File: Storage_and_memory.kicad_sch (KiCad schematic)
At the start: 19 parts, among them J4 DM3AT-SF-PEJM5, U14 SN74AVCA406DGGR, U15 W25Q256JVFIQ

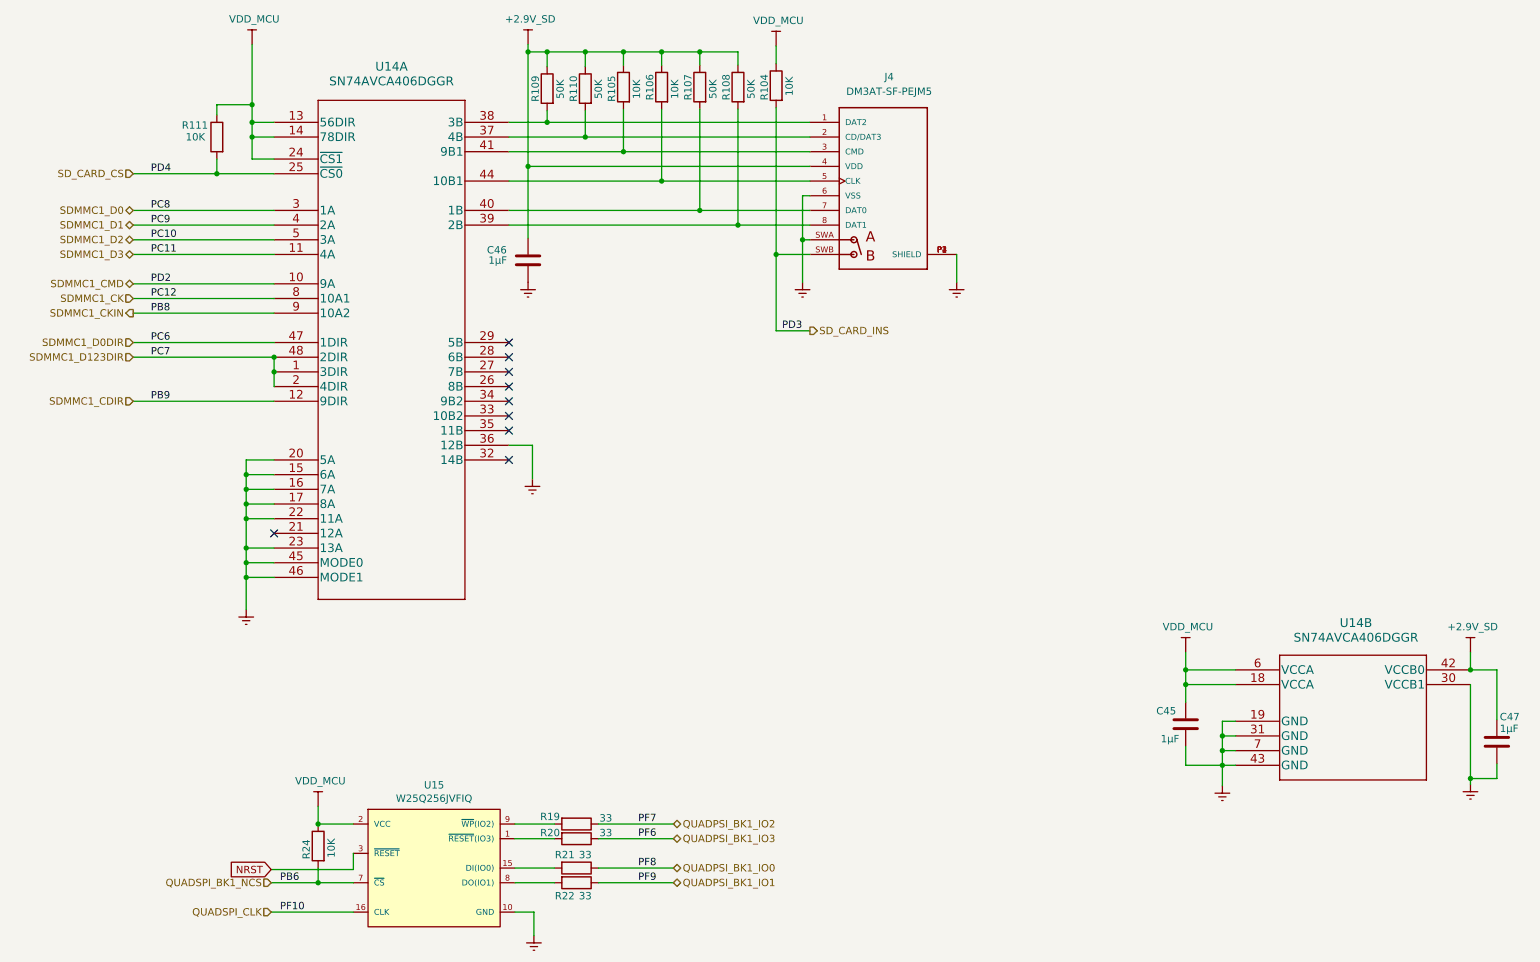
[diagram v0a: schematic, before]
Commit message: KiCAD6.0 scheema rules check done
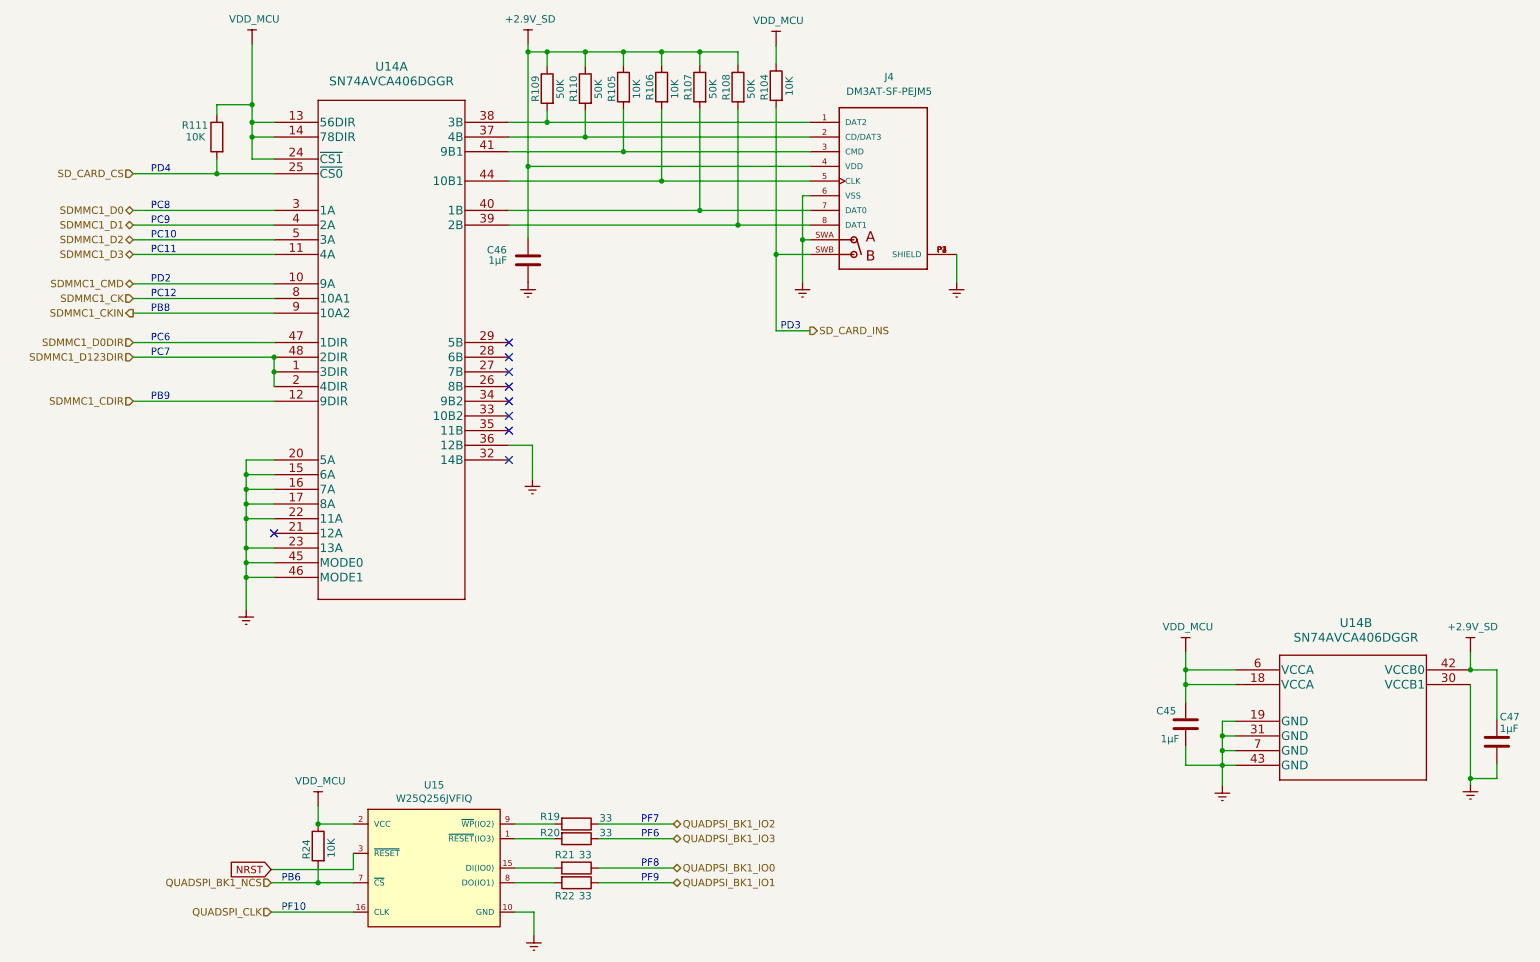
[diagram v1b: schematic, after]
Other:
- note added: "PB6"
- note added: "PB8"
- note added: "PB9"
- note added: "PC10"
- note added: "PC11"
- note added: "PC12"
- note added: "PC6"
- note added: "PC7"
- note added: "PC8"
- note added: "PC9"
- note added: "PD2"
- note added: "PD3"
- note added: "PD4"
- note added: "PF10"
- note added: "PF6"
- note added: "PF7"
- note added: "PF8"
- note added: "PF9"
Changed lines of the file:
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@@
     (stroke (width 0) (type default) (color 0 0 0 0))
   )
-  (label "PC9" (at 45.72 64.262 0)
+  (text "PF10" (at 68.326 183.134 0)
     (effects (font (size 1.27 1.27)) (justify left bottom))
   )
-  (label "PF7" (at 130.048 167.894 0)
+  (text "PD3" (at 154.686 82.55 0)
     (effects (font (size 1.27 1.27)) (justify left bottom))
   )
-  (label "PF9" (at 130.048 178.054 0)
+  (text "PC8" (at 45.72 61.722 0)
     (effects (font (size 1.27 1.27)) (justify left bottom))
   )
-  (label "PD2" (at 45.72 74.422 0)
+  (text "PB6" (at 68.326 178.054 0)
     (effects (font (size 1.27 1.27)) (justify left bottom))
   )
-  (label "PC6" (at 45.72 84.582 0)
+  (text "PC9" (at 45.72 64.262 0)
     (effects (font (size 1.27 1.27)) (justify left bottom))
   )
-  (label "PC11" (at 45.72 69.342 0)
+  (text "PF7" (at 130.556 167.894 0)
     (effects (font (size 1.27 1.27)) (justify left bottom))
   )
-  (label "PC7" (at 45.72 87.122 0)
+  (text "PF8" (at 130.556 175.514 0)
     (effects (font (size 1.27 1.27)) (justify left bottom))
   )
-  (label "PB9" (at 45.72 94.742 0)
+  (text "PF9" (at 130.556 178.054 0)
     (effects (font (size 1.27 1.27)) (justify left bottom))
   )
-  (label "PC8" (at 45.72 61.722 0)
+  (text "PD4" (at 45.72 55.372 0)
     (effects (font (size 1.27 1.27)) (justify left bottom))
   )
-  (label "PC10" (at 45.72 66.802 0)
+  (text "PC12" (at 45.72 76.962 0)
     (effects (font (size 1.27 1.27)) (justify left bottom))
   )
-  (label "PD3" (at 154.94 82.55 0)
+  (text "PF6" (at 130.556 170.434 0)
     (effects (font (size 1.27 1.27)) (justify left bottom))
   )
-  (label "PF8" (at 130.048 175.514 0)
+  (text "PD2" (at 45.72 74.422 0)
     (effects (font (size 1.27 1.27)) (justify left bottom))
   )
-  (label "PC12" (at 45.72 76.962 0)
+  (text "PB9" (at 45.72 94.742 0)
     (effects (font (size 1.27 1.27)) (justify left bottom))
   )
-  (label "PB6" (at 68.072 178.054 0)
+  (text "PC11" (at 45.72 69.342 0)
     (effects (font (size 1.27 1.27)) (justify left bottom))
   )
-  (label "PF10" (at 68.072 183.134 0)
+  (text "PB8" (at 45.72 79.502 0)
     (effects (font (size 1.27 1.27)) (justify left bottom))
   )
-  (label "PD4" (at 45.72 55.372 0)
+  (text "PC7" (at 45.72 87.122 0)
     (effects (font (size 1.27 1.27)) (justify left bottom))
   )
-  (label "PF6" (at 130.048 170.434 0)
+  (text "PC6" (at 45.72 84.582 0)
     (effects (font (size 1.27 1.27)) (justify left bottom))
   )
-  (label "PB8" (at 45.72 79.502 0)
+  (text "PC10" (at 45.72 66.802 0)
     (effects (font (size 1.27 1.27)) (justify left bottom))
   )

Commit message: PCB ver. 0.3
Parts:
- R104, R105, R106, R107, R108, R109, R110, R111: footprint Resistor_SMD:R_0805_2012Metric_Pad1.20x1.40mm_HandSolder -> Resistor_SMD:R_0805_2012Metric
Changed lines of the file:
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@@
       (effects (font (size 1.27 1.27)) (justify left))
     )
-    (property "Footprint" "Resistor_SMD:R_0805_2012Metric_Pad1.20x1.40mm_HandSolder" (id 2) (at 58.928 49.022 90)
+    (property "Footprint" "Resistor_SMD:R_0805_2012Metric" (id 2) (at 58.928 49.022 90)
       (effects (font (size 1.27 1.27)) hide)
     )
@@
       (effects (font (size 1.27 1.27)) (justify left))
     )
-    (property "Footprint" "Resistor_SMD:R_0805_2012Metric_Pad1.20x1.40mm_HandSolder" (id 2) (at 116.078 40.64 90)
+    (property "Footprint" "Resistor_SMD:R_0805_2012Metric" (id 2) (at 116.078 40.64 90)
       (effects (font (size 1.27 1.27)) hide)
     )
@@
       (effects (font (size 1.27 1.27)) (justify left))
     )
-    (property "Footprint" "Resistor_SMD:R_0805_2012Metric_Pad1.20x1.40mm_HandSolder" (id 2) (at 122.682 40.64 90)
+    (property "Footprint" "Resistor_SMD:R_0805_2012Metric" (id 2) (at 122.682 40.64 90)
       (effects (font (size 1.27 1.27)) hide)
     )
@@
       (effects (font (size 1.27 1.27)) (justify left))
     )
-    (property "Footprint" "Resistor_SMD:R_0805_2012Metric_Pad1.20x1.40mm_HandSolder" (id 2) (at 129.286 40.386 90)
+    (property "Footprint" "Resistor_SMD:R_0805_2012Metric" (id 2) (at 129.286 40.386 90)
       (effects (font (size 1.27 1.27)) hide)
     )
@@
       (effects (font (size 1.27 1.27)) (justify left))
     )
-    (property "Footprint" "Resistor_SMD:R_0805_2012Metric_Pad1.20x1.40mm_HandSolder" (id 2) (at 135.89 40.386 90)
+    (property "Footprint" "Resistor_SMD:R_0805_2012Metric" (id 2) (at 135.89 40.386 90)
       (effects (font (size 1.27 1.27)) hide)
     )
@@
       (effects (font (size 1.27 1.27)) (justify left))
     )
-    (property "Footprint" "Resistor_SMD:R_0805_2012Metric_Pad1.20x1.40mm_HandSolder" (id 2) (at 142.494 40.386 90)
+    (property "Footprint" "Resistor_SMD:R_0805_2012Metric" (id 2) (at 142.494 40.386 90)
       (effects (font (size 1.27 1.27)) hide)
     )
@@
       (effects (font (size 1.27 1.27)) (justify left))
     )
-    (property "Footprint" "Resistor_SMD:R_0805_2012Metric_Pad1.20x1.40mm_HandSolder" (id 2) (at 149.098 40.386 90)
+    (property "Footprint" "Resistor_SMD:R_0805_2012Metric" (id 2) (at 149.098 40.386 90)
       (effects (font (size 1.27 1.27)) hide)
     )
@@
       (effects (font (size 1.27 1.27)) (justify left))
     )
-    (property "Footprint" "Resistor_SMD:R_0805_2012Metric_Pad1.20x1.40mm_HandSolder" (id 2) (at 155.702 40.132 90)
+    (property "Footprint" "Resistor_SMD:R_0805_2012Metric" (id 2) (at 155.702 40.132 90)
       (effects (font (size 1.27 1.27)) hide)
     )

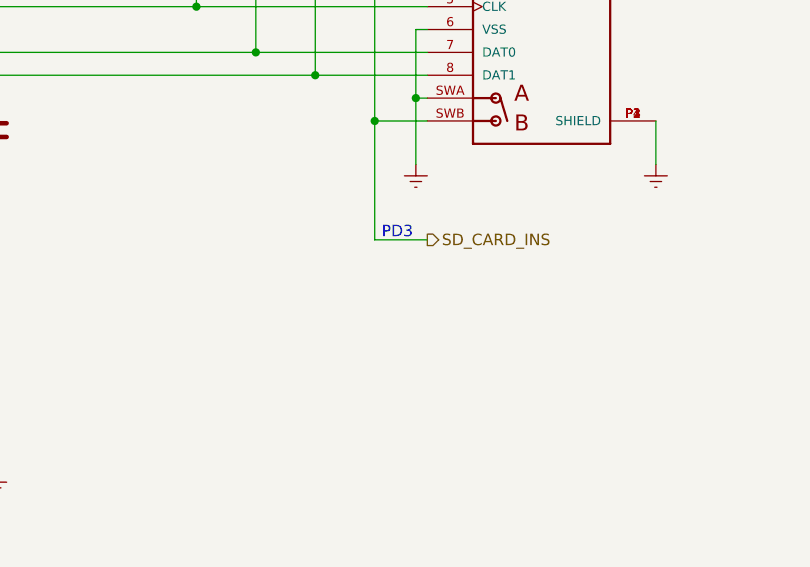
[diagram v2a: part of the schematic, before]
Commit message: GPIO port changed for input signals
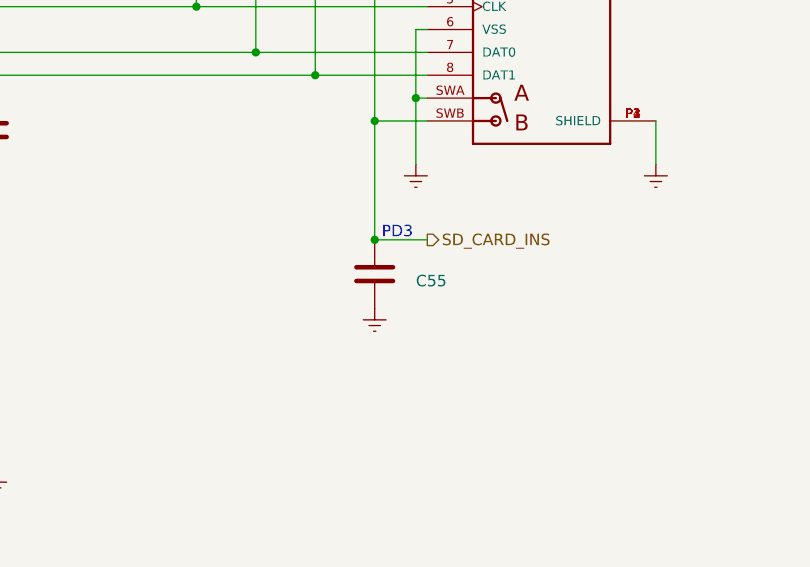
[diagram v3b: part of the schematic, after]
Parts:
- added C55: (no value), symbol Device:C
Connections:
- net GNDREF: now also C55.2
- net SD_CARD_INS: now also C55.1
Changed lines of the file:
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@@
   (junction (at 63.246 43.434) (diameter 0) (color 0 0 0 0)
+  )
+  (junction (at 153.924 82.55) (diameter 0) (color 0 0 0 0)
   )
   (junction (at 57.15 55.372) (diameter 0) (color 0 0 0 0)
@@
     (pin "8")
     (pin "9")
+    (pin "18")
+    (pin "19")
+    (pin "30")
+    (pin "31")
+    (pin "42")
+    (pin "43")
+    (pin "6")
+    (pin "7")
   )
   (symbol (lib_id "SVIELCOM_Library:SN74AVCA406DGGR") (at 233.426 143.764 0) (unit 2)
@@
       (effects (font (size 1.524 1.524)) hide)
     )
+    (pin "1")
+    (pin "10")
+    (pin "11")
+    (pin "12")
+    (pin "13")
+    (pin "14")
+    (pin "15")
+    (pin "16")
+    (pin "17")
+    (pin "2")
+    (pin "20")
+    (pin "21")
+    (pin "22")
+    (pin "23")
+    (pin "24")
+    (pin "25")
+    (pin "26")
+    (pin "27")
+    (pin "28")
+    (pin "29")
+    (pin "3")
+    (pin "32")
+    (pin "33")
+    (pin "34")
+    (pin "35")
+    (pin "36")
+    (pin "37")
+    (pin "38")
+    (pin "39")
+    (pin "4")
+    (pin "40")
+    (pin "41")
+    (pin "44")
+    (pin "45")
+    (pin "46")
+    (pin "47")
+    (pin "48")
+    (pin "5")
+    (pin "8")
+    (pin "9")
     (pin "18")
     (pin "19")
@@
     (pin "1")
   )
+  (symbol (lib_id "power:GNDREF") (at 153.924 90.17 0) (unit 1)
+    (in_bom yes) (on_board yes)
+    (property "Reference" "#PWR075" (id 0) (at 153.924 96.52 0)
+      (effects (font (size 1.27 1.27)) hide)
+    )
+    (property "Value" "GNDREF" (id 1) (at 154.051 93.4212 90)
+      (effects (font (size 1.27 1.27)) (justify right) hide)
+    )
+    (property "Footprint" "" (id 2) (at 153.924 90.17 0)
+      (effects (font (size 1.27 1.27)) hide)
+    )
+    (property "Datasheet" "" (id 3) (at 153.924 90.17 0)
+      (effects (font (size 1.27 1.27)) hide)
+    )
+    (pin "1")
+  )
+  (symbol (lib_id "Device:C") (at 153.924 86.36 0) (unit 1)
+    (in_bom yes) (on_board yes)
+    (property "Reference" "C55" (id 0) (at 158.496 87.122 0)
+      (effects (font (size 1.27 1.27)) (justify left))
+    )
+    (property "Value" "" (id 1) (at 156.464 89.154 0)
+      (effects (font (size 1.27 1.27)) (justify left))
+    )
+    (property "Footprint" "" (id 2) (at 154.8892 90.17 0)
+      (effects (font (size 1.27 1.27)) hide)
+    )
+    (property "Datasheet" "http://www.farnell.com/datasheets/2710676.pdf" (id 3) (at 153.924 86.36 0)
+      (effects (font (size 1.27 1.27)) hide)
+    )
+    (property "Type" "CL10B104KC8NNNC" (id 4) (at 153.924 86.36 0)
+      (effects (font (size 1.27 1.27)) hide)
+    )
+    (pin "1")
+    (pin "2")
+  )
 )

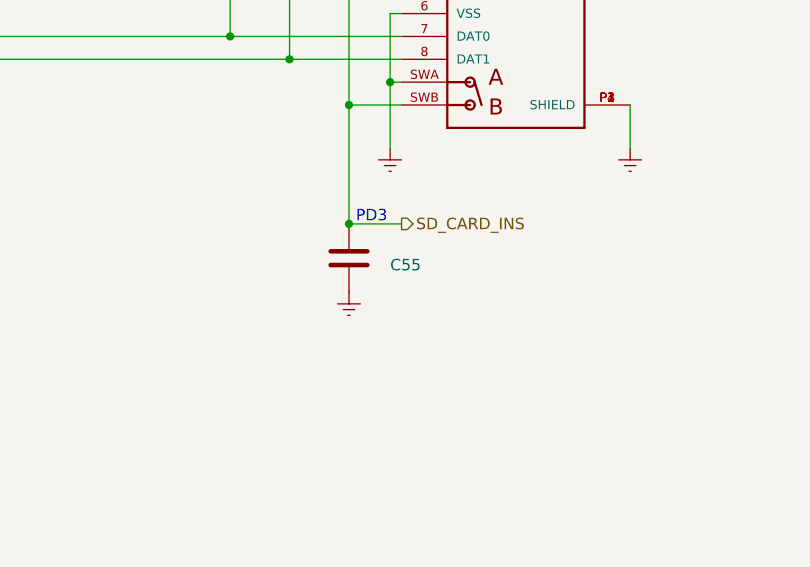
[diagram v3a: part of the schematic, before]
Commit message: External connectors sheet added
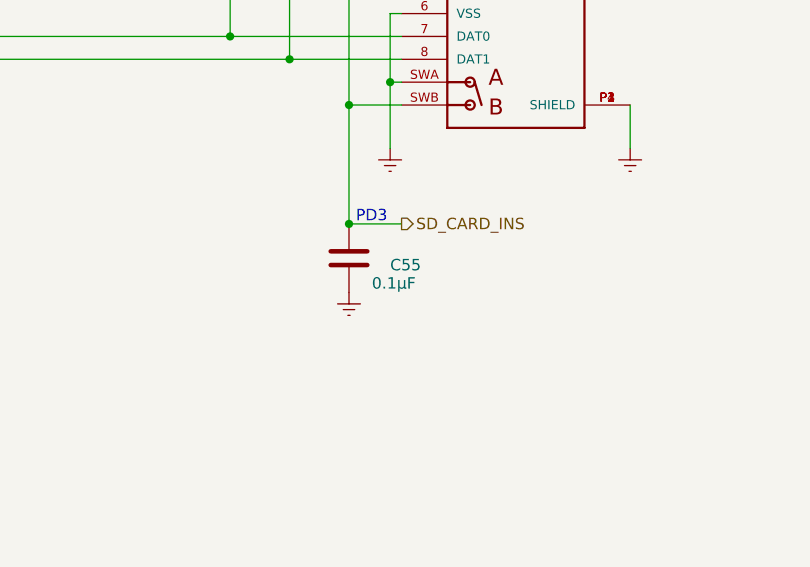
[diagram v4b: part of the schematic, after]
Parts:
- C55: value (none) -> 0.1µF; footprint (none) -> Capacitor_SMD:C_0603_1608Metric
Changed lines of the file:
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@@
       (effects (font (size 1.27 1.27)) (justify left))
     )
-    (property "Value" "" (id 1) (at 156.464 89.154 0)
+    (property "Value" "0.1µF" (id 1) (at 156.464 89.154 0)
       (effects (font (size 1.27 1.27)) (justify left))
     )
-    (property "Footprint" "" (id 2) (at 154.8892 90.17 0)
+    (property "Footprint" "Capacitor_SMD:C_0603_1608Metric" (id 2) (at 154.8892 90.17 0)
       (effects (font (size 1.27 1.27)) hide)
     )

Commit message: All handsolder footprints removed
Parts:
- R24: footprint Resistor_SMD:R_0805_2012Metric_Pad1.20x1.40mm_HandSolder -> Resistor_SMD:R_0805_2012Metric
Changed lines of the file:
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@@
       (effects (font (size 1.27 1.27)) (justify left))
     )
-    (property "Footprint" "Resistor_SMD:R_0805_2012Metric_Pad1.20x1.40mm_HandSolder" (id 2) (at 76.454 171.704 90)
+    (property "Footprint" "Resistor_SMD:R_0805_2012Metric" (id 2) (at 76.454 171.704 90)
       (effects (font (size 1.27 1.27)) hide)
     )
